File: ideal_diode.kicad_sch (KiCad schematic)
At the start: 17 parts

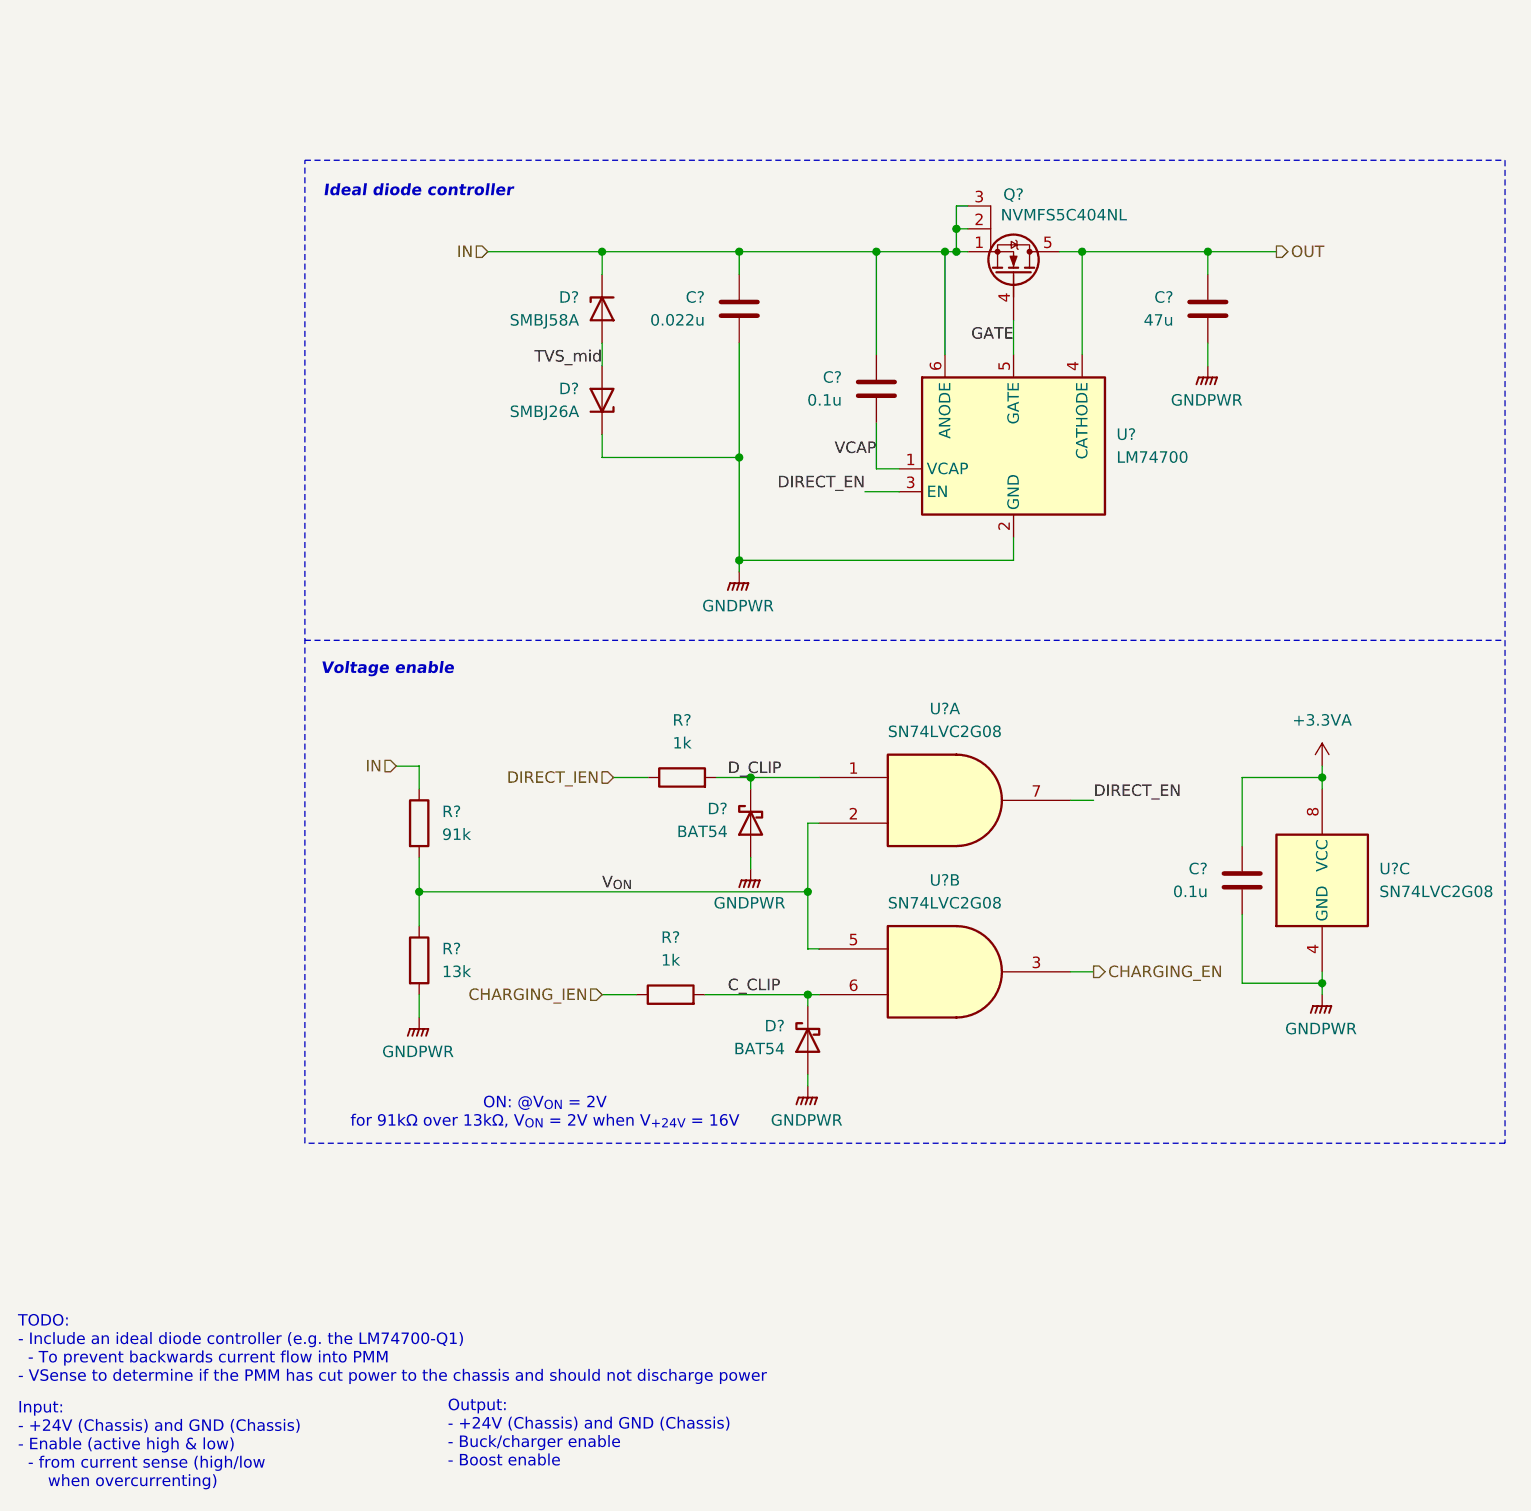
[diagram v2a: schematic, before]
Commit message: Add new components to housekeeping power supply
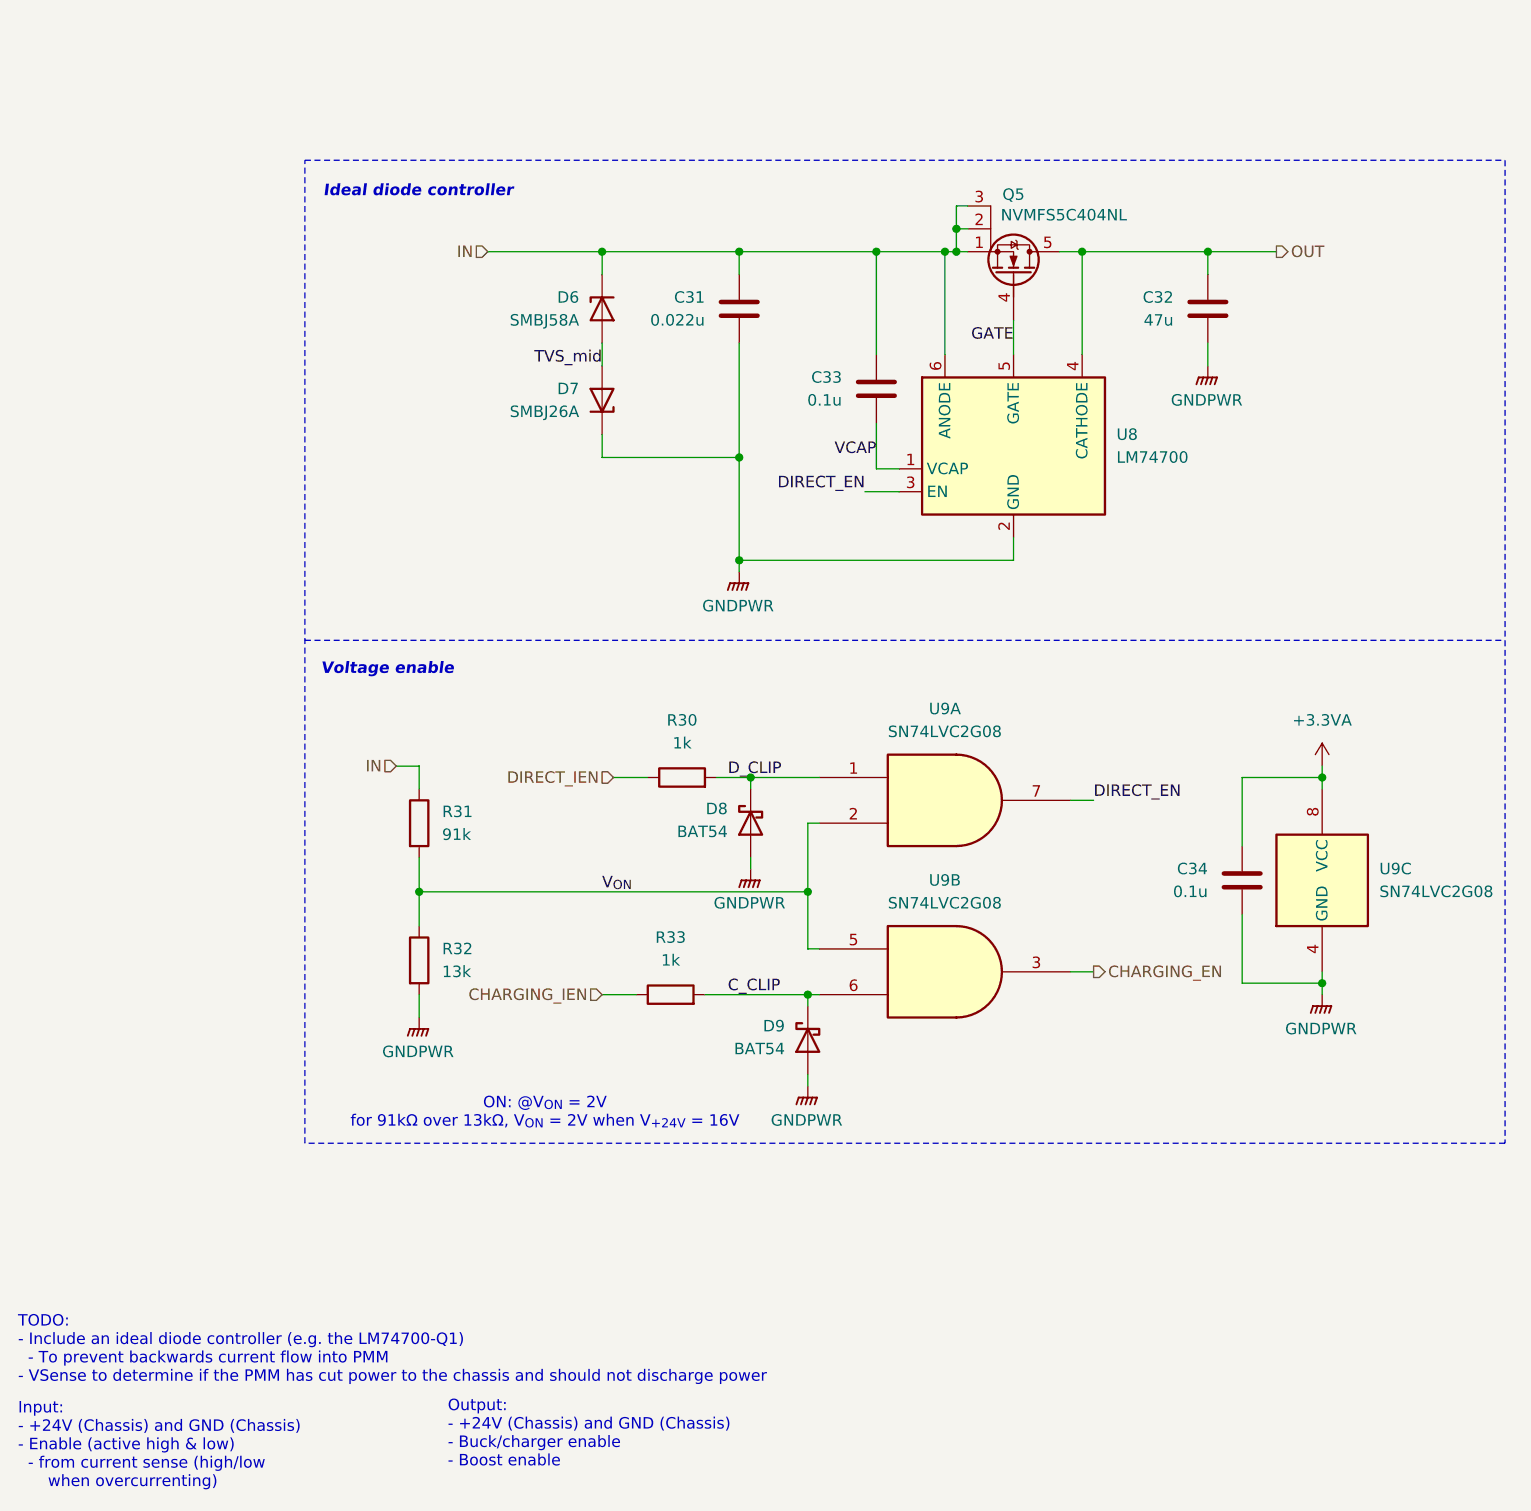
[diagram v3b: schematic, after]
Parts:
- gave numbers to parts that had none: 15

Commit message: began ideal diode layout
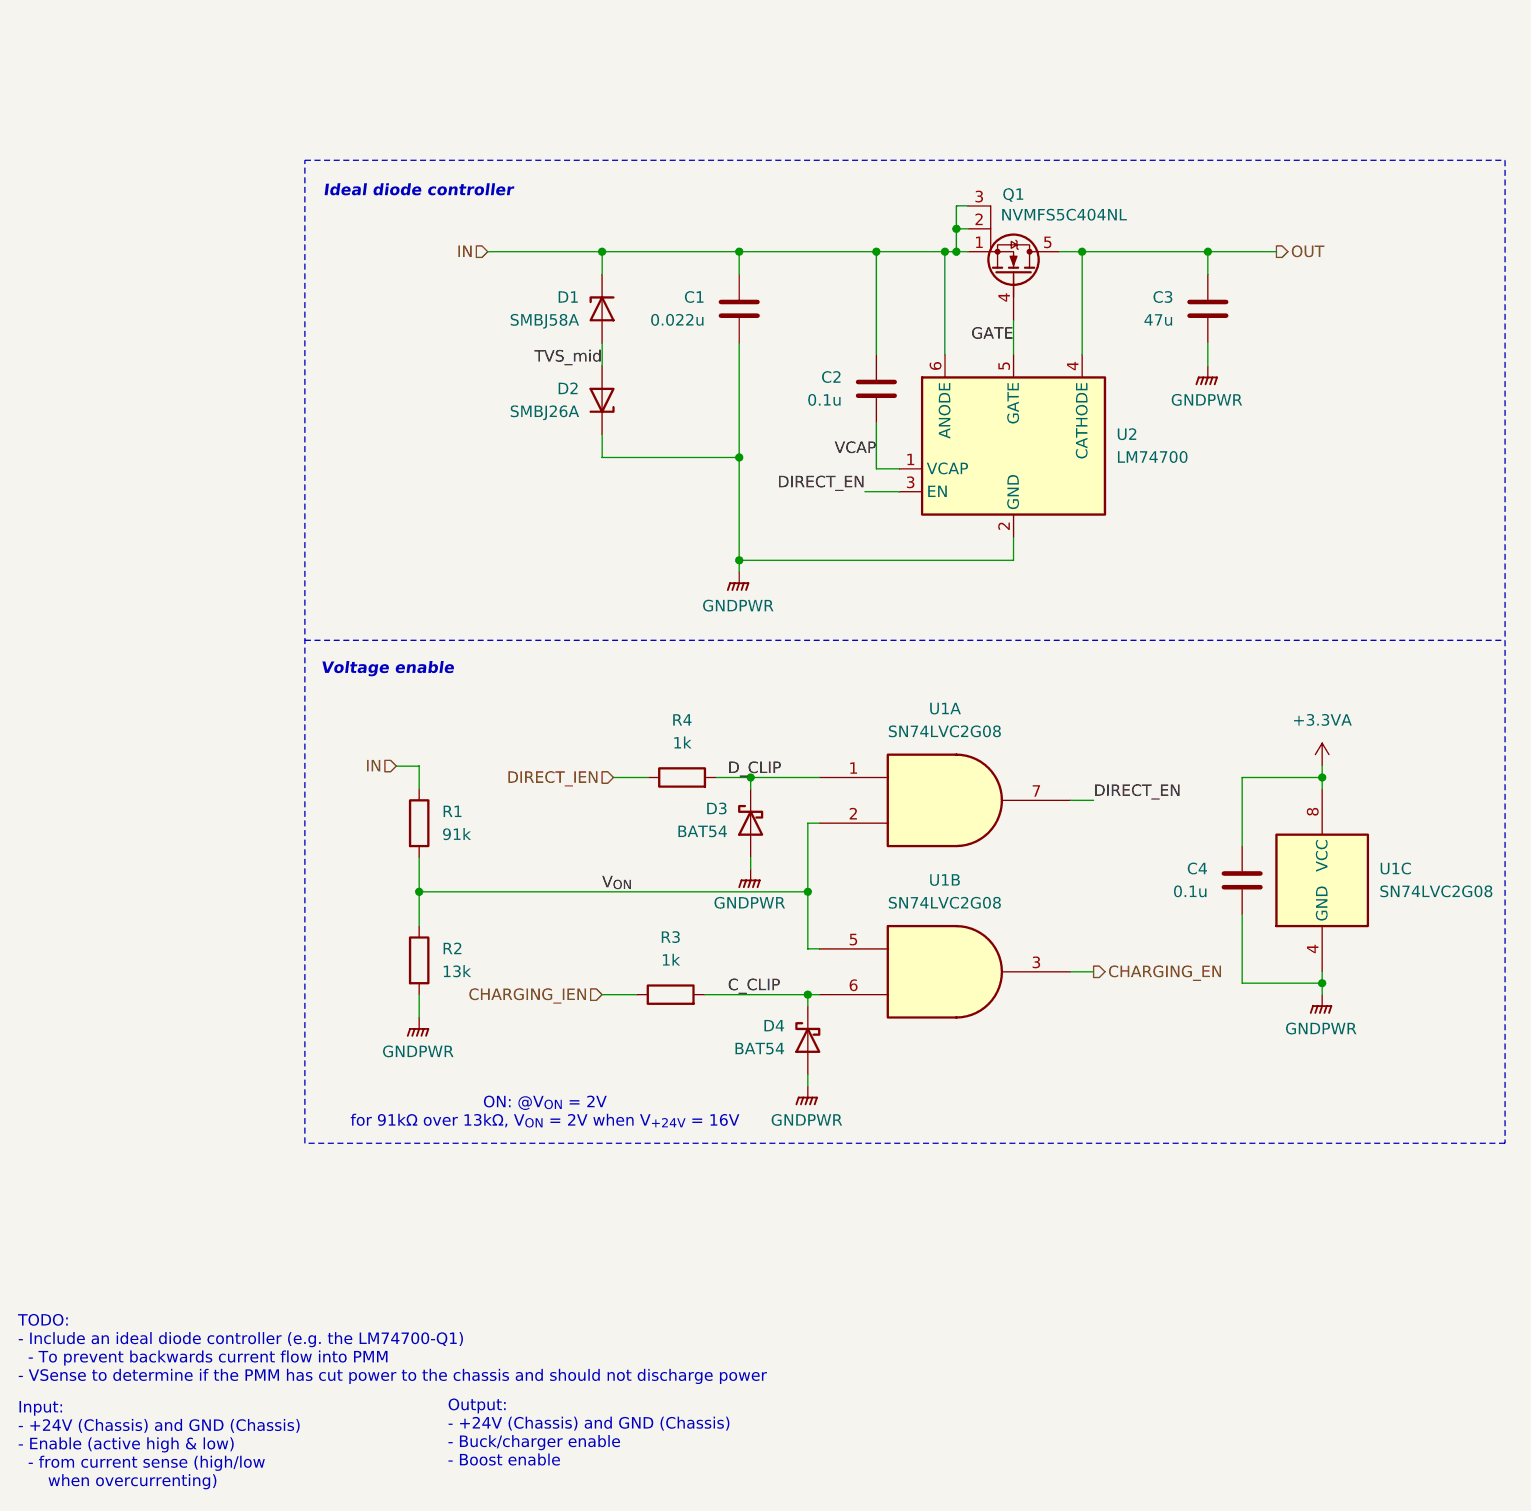
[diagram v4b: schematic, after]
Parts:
- renumbered C31 to C1, C33 to C2, C32 to C3, C34 to C4, D6 to D1, D7 to D2, D8 to D3, D9 to D4, Q5 to Q1, R31 to R1, R32 to R2, R33 to R3, R30 to R4, U9 to U1, U8 to U2
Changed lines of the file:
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@@
 		(dnp no)
 		(fields_autoplaced yes)
-		(property "Reference" "R31"
+		(property "Reference" "R1"
 			(at 91.44 110.4899 0)
 			(effects
@@
 			(project "Ideal Diode Rev1"
 				(path "/1958bbb1-b715-4a10-a229-bee0eabb28b0/4a024d55-f91f-4b32-882f-0df7d5ec96e3"
-					(reference "R?")
+					(reference "R1")
 					(unit 1)
 				)
@@
 		(dnp no)
 		(fields_autoplaced yes)
-		(property "Reference" "R30"
+		(property "Reference" "R4"
 			(at 118.11 100.33 90)
 			(effects
@@
 			(project "Ideal Diode Rev1"
 				(path "/1958bbb1-b715-4a10-a229-bee0eabb28b0/4a024d55-f91f-4b32-882f-0df7d5ec96e3"
-					(reference "R?")
+					(reference "R4")
 					(unit 1)
 				)
@@
 		(on_board yes)
 		(dnp no)
-		(property "Reference" "C32"
+		(property "Reference" "C3"
 			(at 172.72 53.3399 0)
 			(effects
@@
 			(project "Ideal Diode Rev1"
 				(path "/1958bbb1-b715-4a10-a229-bee0eabb28b0/4a024d55-f91f-4b32-882f-0df7d5ec96e3"
-					(reference "C?")
+					(reference "C3")
 					(unit 1)
 				)
@@
 		(on_board yes)
 		(dnp no)
-		(property "Reference" "D8"
+		(property "Reference" "D3"
 			(at 123.19 110.1724 90)
 			(effects
@@
 			(project "Ideal Diode Rev1"
 				(path "/1958bbb1-b715-4a10-a229-bee0eabb28b0/4a024d55-f91f-4b32-882f-0df7d5ec96e3"
-					(reference "D?")
+					(reference "D3")
 					(unit 1)
 				)
@@
 		(on_board yes)
 		(dnp no)
-		(property "Reference" "C31"
+		(property "Reference" "C1"
 			(at 120.65 53.3399 0)
 			(effects
@@
 			(project "Ideal Diode Rev1"
 				(path "/1958bbb1-b715-4a10-a229-bee0eabb28b0/4a024d55-f91f-4b32-882f-0df7d5ec96e3"
-					(reference "C?")
+					(reference "C1")
 					(unit 1)
 				)
@@
 		(on_board yes)
 		(dnp no)
-		(property "Reference" "D9"
+		(property "Reference" "D4"
 			(at 129.54 134.3024 90)
 			(effects
@@
 			(project "Ideal Diode Rev1"
 				(path "/1958bbb1-b715-4a10-a229-bee0eabb28b0/4a024d55-f91f-4b32-882f-0df7d5ec96e3"
-					(reference "D?")
+					(reference "D4")
 					(unit 1)
 				)
@@
 		(dnp no)
 		(fields_autoplaced yes)
-		(property "Reference" "#PWR056"
+		(property "Reference" "#PWR0102"
 			(at 125.73 121.92 0)
 			(effects
@@
 			(project "Ideal Diode Rev1"
 				(path "/1958bbb1-b715-4a10-a229-bee0eabb28b0/4a024d55-f91f-4b32-882f-0df7d5ec96e3"
-					(reference "#PWR?")
+					(reference "#PWR0102")
 					(unit 1)
 				)
@@
 		(dnp no)
 		(fields_autoplaced yes)
-		(property "Reference" "R33"
+		(property "Reference" "R3"
 			(at 116.84 124.46 90)
 			(effects
@@
 			(project "Ideal Diode Rev1"
 				(path "/1958bbb1-b715-4a10-a229-bee0eabb28b0/4a024d55-f91f-4b32-882f-0df7d5ec96e3"
-					(reference "R?")
+					(reference "R3")
 					(unit 1)
 				)
@@
 		(dnp no)
 		(fields_autoplaced yes)
-		(property "Reference" "U9"
+		(property "Reference" "U1"
 			(at 147.3089 118.11 0)
 			(effects
@@
 			(project "Ideal Diode Rev1"
 				(path "/1958bbb1-b715-4a10-a229-bee0eabb28b0/4a024d55-f91f-4b32-882f-0df7d5ec96e3"
-					(reference "U?")
+					(reference "U1")
 					(unit 2)
 				)
@@
 		(dnp no)
 		(fields_autoplaced yes)
-		(property "Reference" "#PWR057"
+		(property "Reference" "#PWR0106"
 			(at 189.23 135.89 0)
 			(effects
@@
 			(project "Ideal Diode Rev1"
 				(path "/1958bbb1-b715-4a10-a229-bee0eabb28b0/4a024d55-f91f-4b32-882f-0df7d5ec96e3"
-					(reference "#PWR?")
+					(reference "#PWR0106")
 					(unit 1)
 				)
@@
 		(dnp no)
 		(fields_autoplaced yes)
-		(property "Reference" "#PWR055"
+		(property "Reference" "#PWR0105"
 			(at 189.23 109.22 0)
 			(effects
@@
 			(project "Ideal Diode Rev1"
 				(path "/1958bbb1-b715-4a10-a229-bee0eabb28b0/4a024d55-f91f-4b32-882f-0df7d5ec96e3"
-					(reference "#PWR?")
+					(reference "#PWR0105")
 					(unit 1)
 				)
@@
 		(dnp no)
 		(fields_autoplaced yes)
-		(property "Reference" "#PWR054"
+		(property "Reference" "#PWR0107"
 			(at 124.46 88.9 0)
 			(effects
@@
 			(project "Ideal Diode Rev1"
 				(path "/1958bbb1-b715-4a10-a229-bee0eabb28b0/4a024d55-f91f-4b32-882f-0df7d5ec96e3"
-					(reference "#PWR?")
+					(reference "#PWR0107")
 					(unit 1)
 				)
@@
 		(on_board yes)
 		(dnp no)
-		(property "Reference" "C33"
+		(property "Reference" "C2"
 			(at 135.89 62.2299 0)
 			(effects
@@
 			(project "Ideal Diode Rev1"
 				(path "/1958bbb1-b715-4a10-a229-bee0eabb28b0/4a024d55-f91f-4b32-882f-0df7d5ec96e3"
-					(reference "C?")
+					(reference "C2")
 					(unit 1)
 				)
@@
 		(on_board yes)
 		(dnp no)
-		(property "Reference" "Q5"
+		(property "Reference" "Q1"
 			(at 154.94 41.91 90)
 			(effects
@@
 			(project "Ideal Diode Rev1"
 				(path "/1958bbb1-b715-4a10-a229-bee0eabb28b0/4a024d55-f91f-4b32-882f-0df7d5ec96e3"
-					(reference "Q?")
+					(reference "Q1")
 					(unit 1)
 				)
@@
 		(dnp no)
 		(fields_autoplaced yes)
-		(property "Reference" "U8"
+		(property "Reference" "U2"
 			(at 166.37 68.5799 0)
 			(effects
@@
 			(project "Ideal Diode Rev1"
 				(path "/1958bbb1-b715-4a10-a229-bee0eabb28b0/4a024d55-f91f-4b32-882f-0df7d5ec96e3"
-					(reference "U?")
+					(reference "U2")
 					(unit 1)
 				)
@@
 		(dnp no)
 		(fields_autoplaced yes)
-		(property "Reference" "U9"
+		(property "Reference" "U1"
 			(at 195.58 116.8399 0)
 			(effects
@@
 			(project "Ideal Diode Rev1"
 				(path "/1958bbb1-b715-4a10-a229-bee0eabb28b0/4a024d55-f91f-4b32-882f-0df7d5ec96e3"
-					(reference "U?")
+					(reference "U1")
 					(unit 3)
 				)
@@
 		(dnp no)
 		(fields_autoplaced yes)
-		(property "Reference" "R32"
+		(property "Reference" "R2"
 			(at 91.44 125.7299 0)
 			(effects
@@
 			(project "Ideal Diode Rev1"
 				(path "/1958bbb1-b715-4a10-a229-bee0eabb28b0/4a024d55-f91f-4b32-882f-0df7d5ec96e3"
-					(reference "R?")
+					(reference "R2")
 					(unit 1)
 				)
@@
 		(on_board yes)
 		(dnp no)
-		(property "Reference" "D6"
+		(property "Reference" "D1"
 			(at 106.68 53.3399 90)
 			(effects
@@
 			(project "Ideal Diode Rev1"
 				(path "/1958bbb1-b715-4a10-a229-bee0eabb28b0/4a024d55-f91f-4b32-882f-0df7d5ec96e3"
-					(reference "D?")
+					(reference "D1")
 					(unit 1)
 				)
@@
 		(dnp no)
 		(fields_autoplaced yes)
-		(property "Reference" "#PWR053"
+		(property "Reference" "#PWR0104"
 			(at 176.53 66.04 0)
 			(effects
@@
 			(project "Ideal Diode Rev1"
 				(path "/1958bbb1-b715-4a10-a229-bee0eabb28b0/4a024d55-f91f-4b32-882f-0df7d5ec96e3"
-					(reference "#PWR?")
+					(reference "#PWR0104")
 					(unit 1)
 				)
@@
 		(on_board yes)
 		(dnp no)
-		(property "Reference" "C34"
+		(property "Reference" "C4"
 			(at 176.53 116.8399 0)
 			(effects
@@
 			(project "Ideal Diode Rev1"
 				(path "/1958bbb1-b715-4a10-a229-bee0eabb28b0/4a024d55-f91f-4b32-882f-0df7d5ec96e3"
-					(reference "C?")
+					(reference "C4")
 					(unit 1)
 				)
@@
 		(dnp no)
 		(fields_autoplaced yes)
-		(property "Reference" "U9"
+		(property "Reference" "U1"
 			(at 147.3089 99.06 0)
 			(effects
@@
 			(project "Ideal Diode Rev1"
 				(path "/1958bbb1-b715-4a10-a229-bee0eabb28b0/4a024d55-f91f-4b32-882f-0df7d5ec96e3"
-					(reference "U?")
+					(reference "U1")
 					(unit 1)
 				)
@@
 		(dnp no)
 		(fields_autoplaced yes)
-		(property "Reference" "#PWR058"
+		(property "Reference" "#PWR0103"
 			(at 88.9 138.43 0)
 			(effects
@@
 			(project "Ideal Diode Rev1"
 				(path "/1958bbb1-b715-4a10-a229-bee0eabb28b0/4a024d55-f91f-4b32-882f-0df7d5ec96e3"
-					(reference "#PWR?")
+					(reference "#PWR0103")
 					(unit 1)
 				)
@@
 		(on_board yes)
 		(dnp no)
-		(property "Reference" "D7"
+		(property "Reference" "D2"
 			(at 106.68 63.4999 90)
 			(effects
@@
 			(project "Ideal Diode Rev1"
 				(path "/1958bbb1-b715-4a10-a229-bee0eabb28b0/4a024d55-f91f-4b32-882f-0df7d5ec96e3"
-					(reference "D?")
+					(reference "D2")
 					(unit 1)
 				)
@@
 		(dnp no)
 		(fields_autoplaced yes)
-		(property "Reference" "#PWR059"
+		(property "Reference" "#PWR0101"
 			(at 132.08 146.05 0)
 			(effects
@@
 			(project "Ideal Diode Rev1"
 				(path "/1958bbb1-b715-4a10-a229-bee0eabb28b0/4a024d55-f91f-4b32-882f-0df7d5ec96e3"
-					(reference "#PWR?")
-					(unit 1)
-				)
+					(reference "#PWR0101")
+					(unit 1)
+				)
